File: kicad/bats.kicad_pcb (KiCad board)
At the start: 2 copper layers, 68.9 x 53.6 mm, 30 parts, among them P1 SERVO, SW1 RESET, SW2 SHOT, SW3 UP, SW4 LEFT, SW5 DOWN, SW6 RIGHT, U1 BUZZER

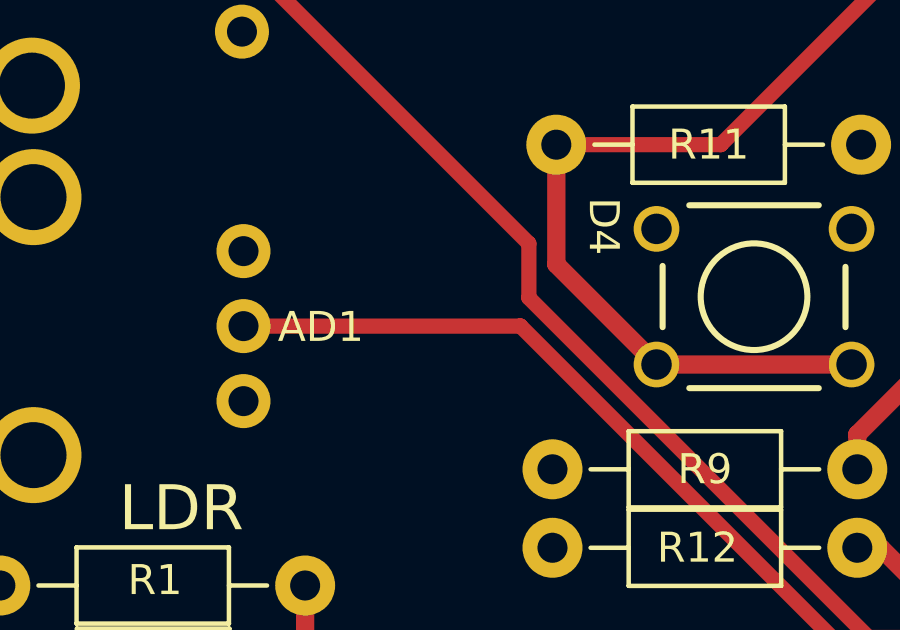
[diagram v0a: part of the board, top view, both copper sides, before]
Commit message: Engadida unha conexión extra na area positiva.
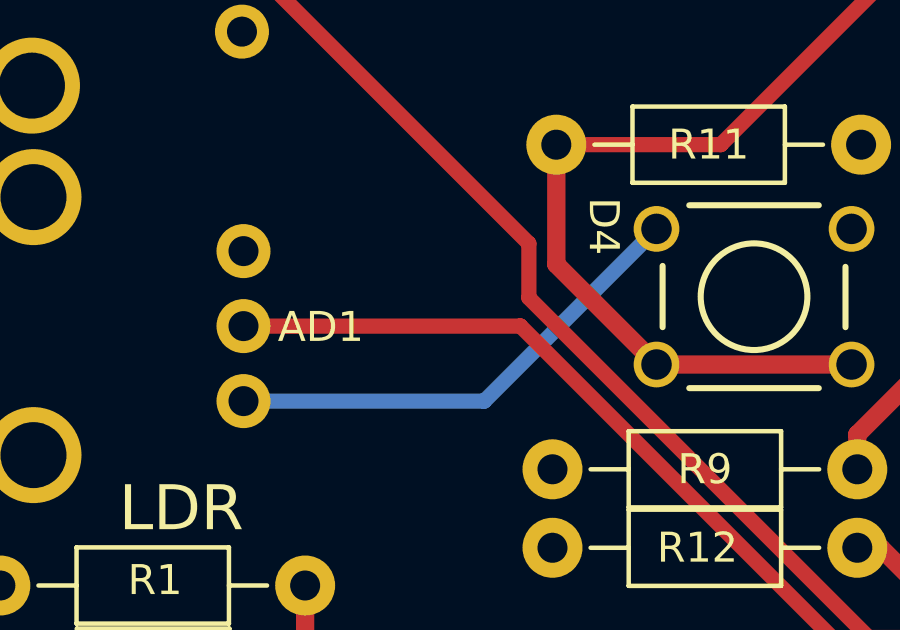
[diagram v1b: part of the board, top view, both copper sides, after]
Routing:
- net /VCC: track 18.5 -> 34.7 mm
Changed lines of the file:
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@@
     (thickness 1.6)
     (drawings 30)
-    (tracks 118)
+    (tracks 120)
     (zones 0)
     (modules 30)
@@
   (layers
     (0 F.Cu signal)
-    (31 B.Cu signal hide)
+    (31 B.Cu signal)
     (32 B.Adhes user hide)
     (33 F.Adhes user hide)
     (34 B.Paste user hide)
     (35 F.Paste user hide)
-    (36 B.SilkS user hide)
+    (36 B.SilkS user)
     (37 F.SilkS user)
-    (38 B.Mask user hide)
-    (39 F.Mask user hide)
+    (38 B.Mask user)
+    (39 F.Mask user)
     (40 Dwgs.User user hide)
     (41 Cmts.User user hide)
     (42 Eco1.User user hide)
     (43 Eco2.User user hide)
-    (44 Edge.Cuts user hide)
+    (44 Edge.Cuts user)
     (45 Margin user hide)
     (46 B.CrtYd user hide)
@@
       (drillshape 0)
       (scaleselection 1)
-      (outputdirectory ../exports/BATS.grb/))
+      (outputdirectory /home/salvari/work/repos/BricoLabs/bats/exports/BATS.svg/))
   )
   (net 0 "")
@@
   (segment (start 159.73044 120.0912) (end 156.39034 116.7511) (width 0.6096) (layer F.Cu) (net 19))
   (segment (start 156.39034 116.7511) (end 156.39034 112.7633) (width 0.6096) (layer F.Cu) (net 19))
+  (segment (start 159.73044 115.57) (end 153.9894 121.31104) (width 0.508) (layer B.Cu) (net 35))
+  (segment (start 153.9894 121.31104) (end 145.9634 121.31104) (width 0.508) (layer B.Cu) (net 35))
   (segment (start 179.87264 98.50628) (end 173.833789 104.545131) (width 0.6096) (layer B.Cu) (net 35))
   (segment (start 173.833789 104.545131) (end 173.833789 107.353101) (width 0.6096) (layer B.Cu) (net 35))

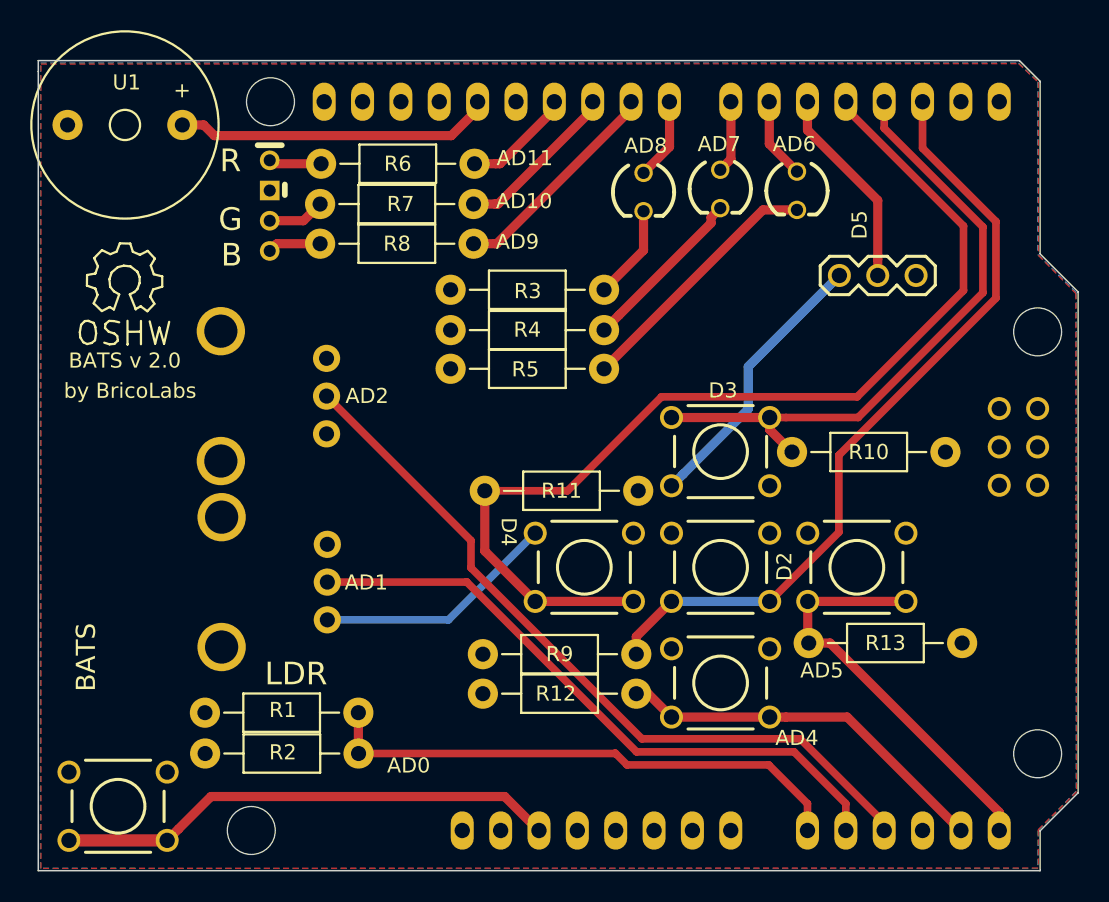
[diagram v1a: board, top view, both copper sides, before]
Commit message: Cambiadas as pegadas das resistencias a furados mais pequenos.
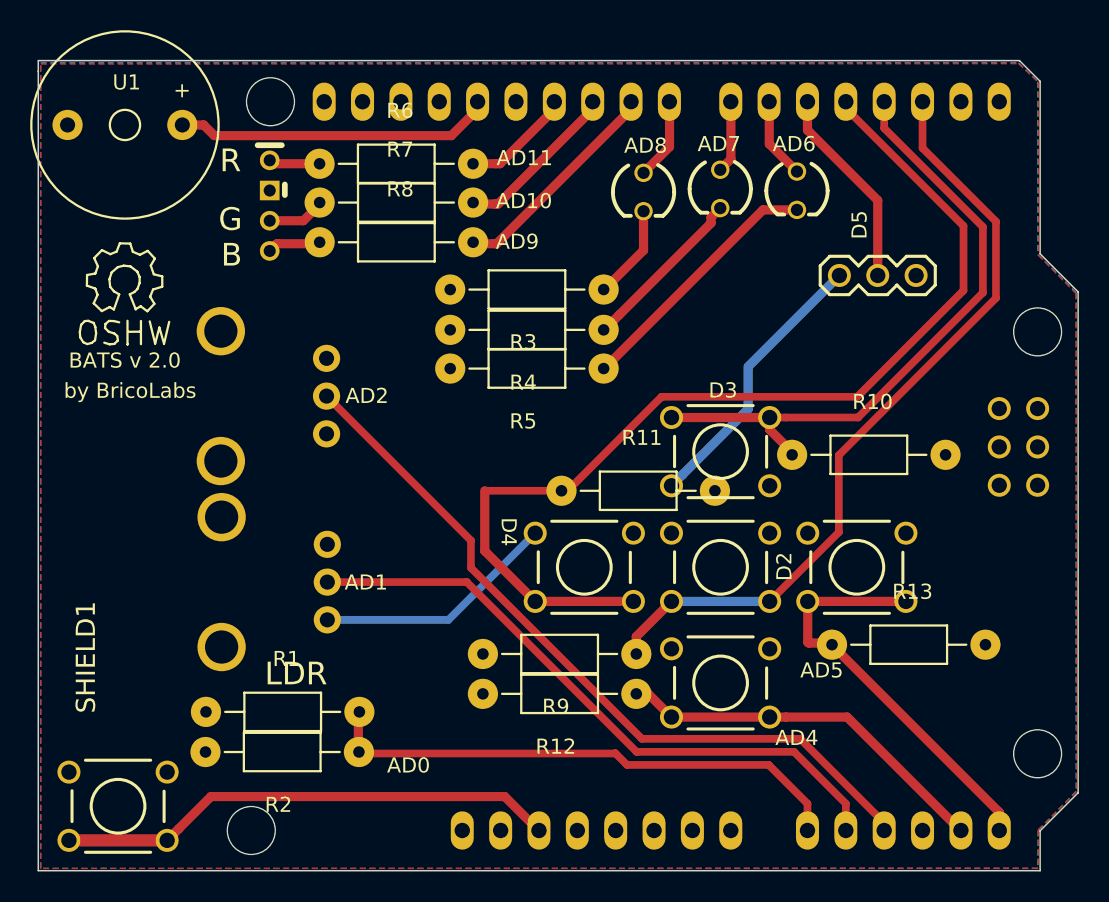
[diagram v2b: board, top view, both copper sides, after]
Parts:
- R1, R10, R11, R12, R13, R2, R3, R4, R5, R6, R7, R8, R9: footprint Resistors_ThroughHole:Resistor_Horizontal_RM10mm -> extra:Resistor_Horizontal_SmallHole_RM10mm
- moved R6 5.18 mm to (145.5, 91.1)
- moved R7 5.11 mm to (145.5, 93.7)
- moved R8 5.11 mm to (145.5, 96.3)
- moved R2 5.11 mm to (148.1, 130.1)
- moved R12 5.08 mm to (166.4, 126.2)
- moved R9 5.08 mm to (166.4, 123.6)
- moved R10 5.08 mm to (176.7, 110.4)
- moved R3 5.05 mm to (164.3, 99.4)
- moved R4 5.05 mm to (164.3, 102.1)
- moved R5 5.05 mm to (164.3, 104.7)
- moved R1 5.01 mm to (137.9, 127.4)
- moved R13 3.54 mm to (179.4, 123.0)
- renumbered BATS to SHIELD1

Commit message: - Correxida a posición da rotulacion de todas as resistencias - Cambiada o tamaño dos leds a 5 mm, cambia tamén a sua posición, pecha o issue #4 - Cambiada a posición de resistencias R3, R4 e R5 e mais a posición do   conector do servo - Declaramos pechado o issue #8 relativo a furados mais pequenos nas   pegadas das resistencias - Solventado o issue#10 relativo a zona aillada na pista frontal
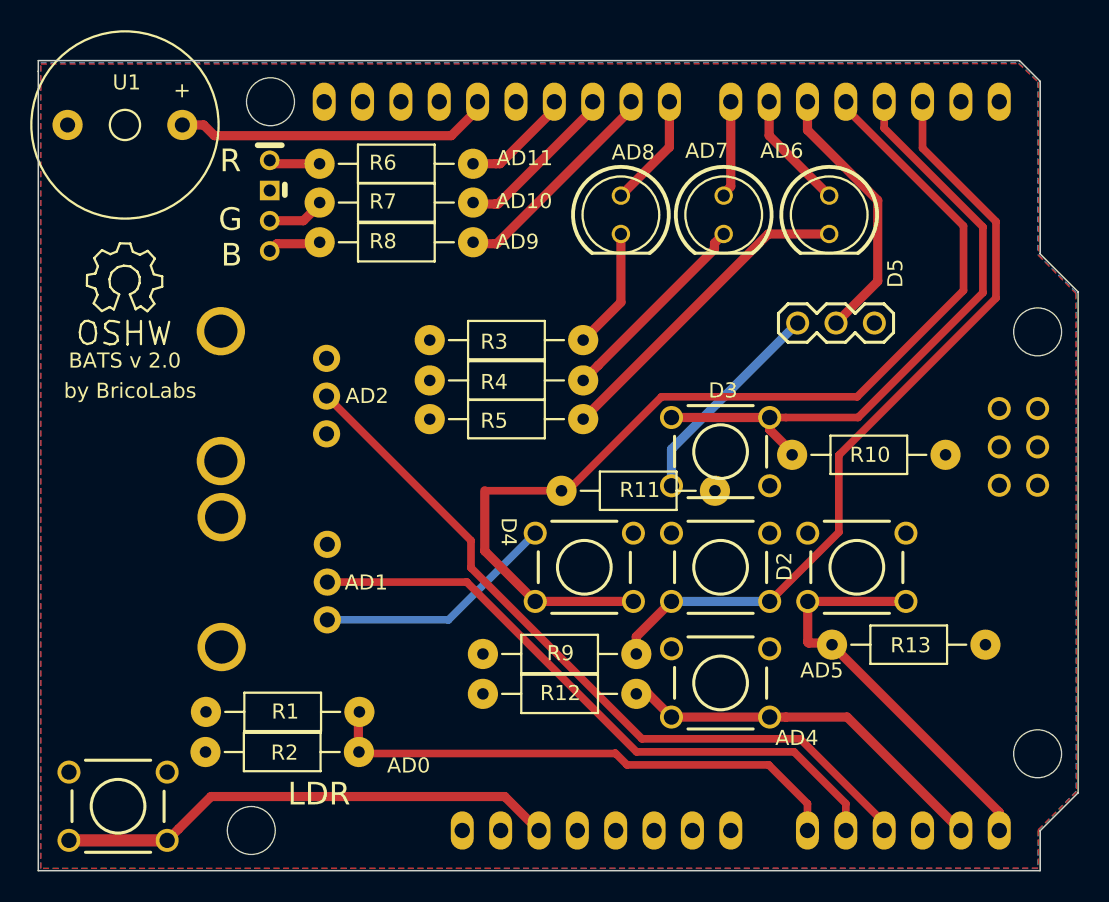
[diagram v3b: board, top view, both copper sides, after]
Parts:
- LED1, LED2, LED3: footprint FT:LED-3MM -> FT:LED-5MM
- moved P1 4.19 mm to (177.1, 101.7)
- moved R3 3.61 mm to (162.9, 102.8)
- moved R4 3.61 mm to (162.9, 105.5)
- moved R5 3.61 mm to (162.9, 108.0)
- moved LED3 2.66 mm to (179.2, 94.5)
- moved LED1 2.13 mm to (165.4, 94.5)
- moved LED2 1.73 mm to (172.2, 94.5)
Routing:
- net /VCC: track 34.7 -> 30.4 mm
- net /ARD5: track 13.5 -> 17.7 mm
- net Net-(LED3-PadK): track 17.1 -> 21.4 mm
- net /ARD6: track 5.41 -> 7.87 mm
- net Net-(LED2-PadK): track 11.3 -> 13.6 mm
- net /ARD8: track 5.46 -> 7.55 mm
- net Net-(LED1-PadK): track 6.29 -> 8.06 mm
- net /ARD7: track 4.83 -> 6.27 mm

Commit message: Versión 2.1, non é outra cousa que a versión 2.0 cos erros correxidos
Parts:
- BATS v 2.1: renamed from BATS v 2.0
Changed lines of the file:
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@@
     (links 67)
     (no_connects 0)
-    (area 126.772199 84.227199 195.731601 137.972001)
+    (area 120.578067 81.661 196.085461 138.40568)
     (thickness 1.6)
     (drawings 30)
@@
     (visible_elements FFFFEF7F)
     (pcbplotparams
-      (layerselection 0x010f0_ffffffff)
+      (layerselection 0x011f0_ffffffff)
       (usegerberextensions false)
       (excludeedgelayer true)
@@
       (drillshape 0)
       (scaleselection 1)
-      (outputdirectory /home/salvari/work/repos/BricoLabs/BATS/exports/BATS.grb/))
+      (outputdirectory /home/salvari/work/repos/BricoLabs/BATS/exports/BATS.svg/SVG_color/))
   )
   (net 0 "")
@@
     (descr "Symbol, OSHW-Logo, Silk Screen,")
     (tags "Symbol, OSHW-Logo, Silk Screen,")
-    (fp_text reference "BATS v 2.0" (at 0.02032 5.28828) (layer F.SilkS)
+    (fp_text reference "BATS v 2.1" (at 0.02032 5.28828) (layer F.SilkS)
       (effects (font (size 1 1) (thickness 0.15)))
     )

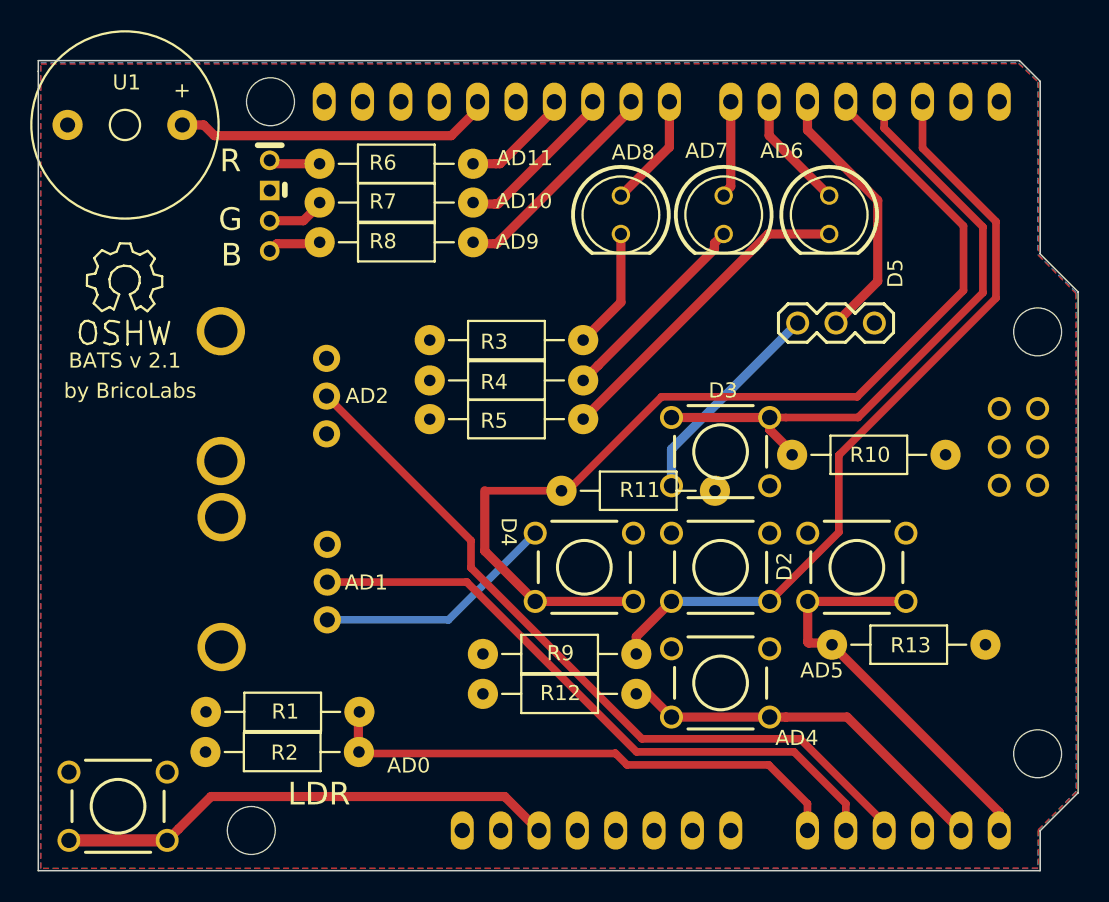
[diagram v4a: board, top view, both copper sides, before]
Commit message: Primeira versión con tres botóns. Ten pistas redundantes e hai que cambiar os pines dos botóns.
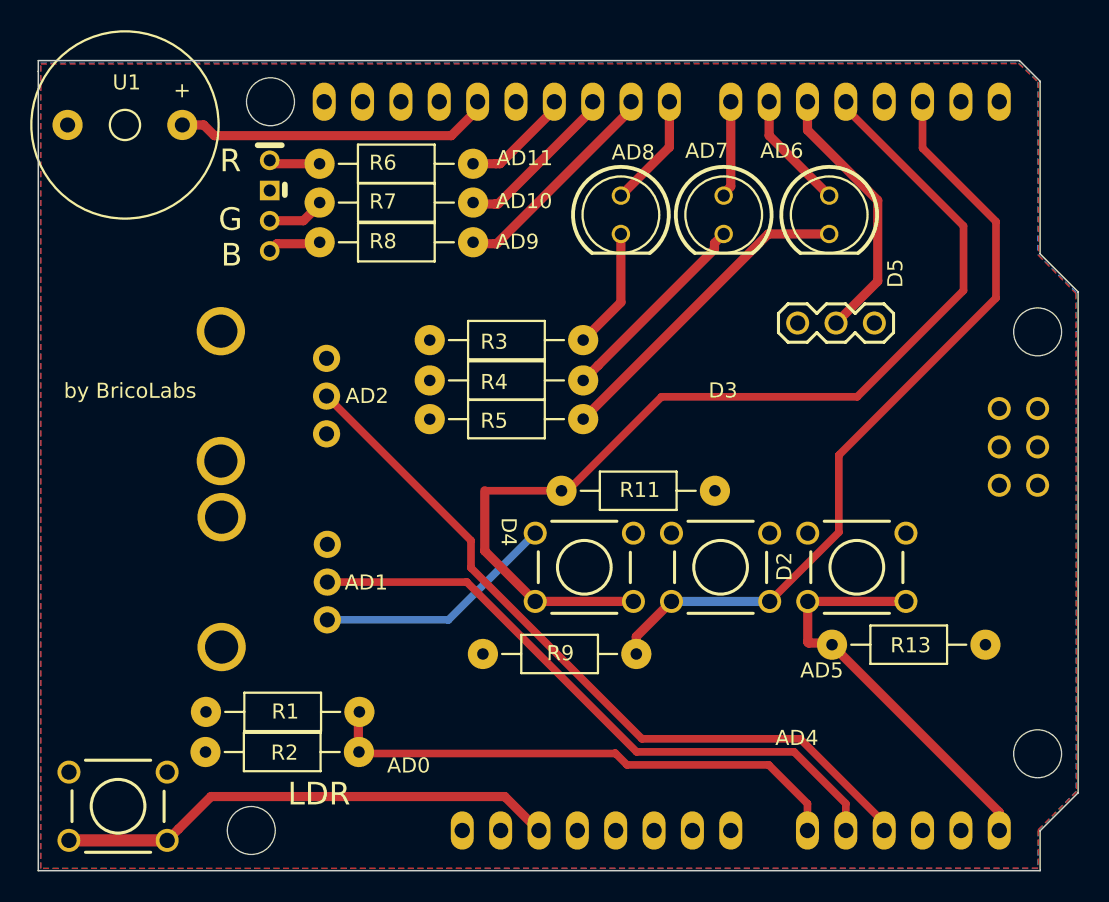
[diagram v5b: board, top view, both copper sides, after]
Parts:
- removed BATS v 2.1: Symbol_OSHW-Logo_SilkScreen, Symbols:Symbol_OSHW-Logo_SilkScreen
- removed G***: LOGO, silklibrary:bat_b
- removed R10, R12: 10K, extra:Resistor_Horizontal_SmallHole_RM10mm
- removed SW3: UP, FT:SW_PUSHBUTTON_PTH
- removed SW5: DOWN, FT:SW_PUSHBUTTON_PTH
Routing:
- net /ARD3: track 42.3 -> 0.00 mm
- net /AD4: track 25.2 -> 0.02 mm
- net /VCC: track 30.4 -> 16.1 mm

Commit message: Amañados os terminais dos botóns Compre rotar os botóns para simplificar as pistas
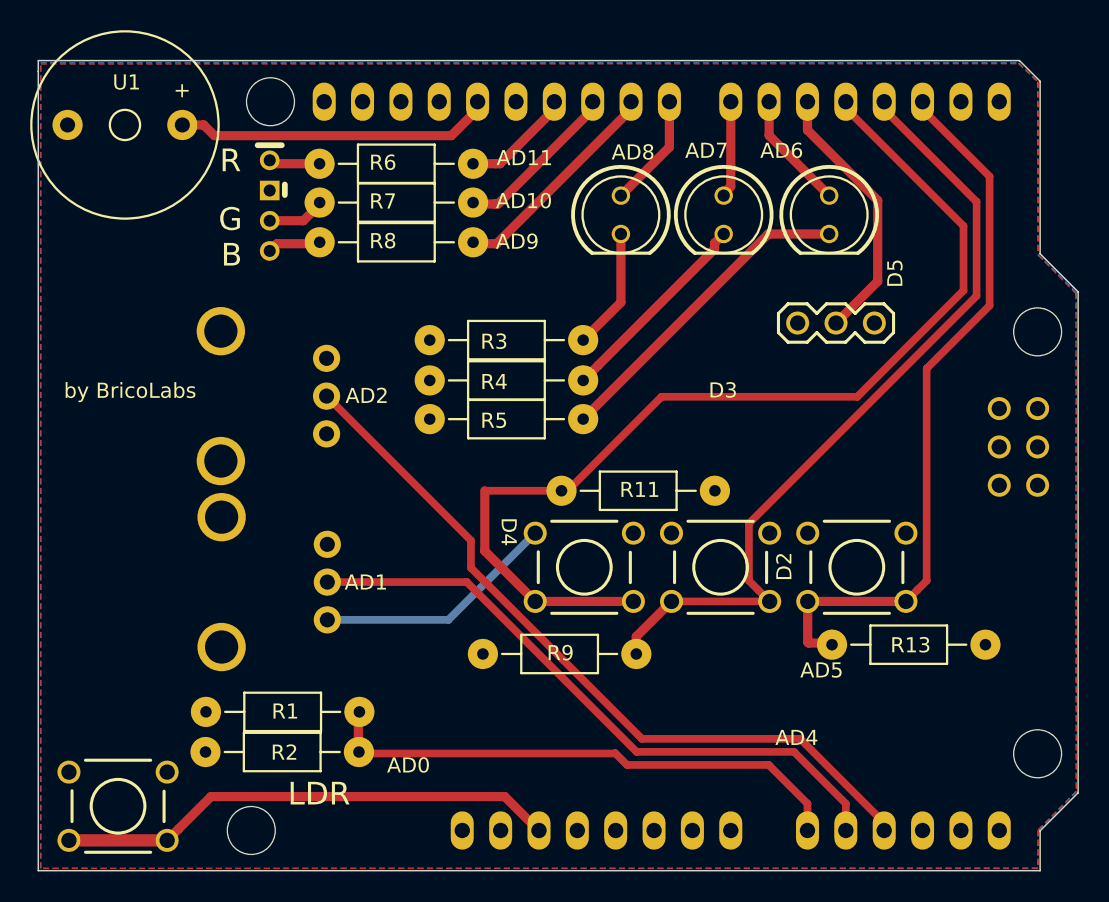
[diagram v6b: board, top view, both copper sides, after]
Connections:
- net /AD4 renamed Net-(SHIELD1-PadAD4)
- R13 pad 1: /AD5 -> /ARD2
- R9 pad 1: /ARD2 -> /ARD3
- SHIELD1 pad AD5: /AD5 -> Net-(SHIELD1-PadAD5)
- SW2 pad 2: /ARD2 -> /ARD3
- SW6 pad 2: /AD5 -> /ARD2
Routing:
- net /ARD3: track 0.00 -> 53.4 mm
- net /AD5: track 27.8 -> 0.00 mm
- net /ARD2: track 52.3 -> 47.9 mm
